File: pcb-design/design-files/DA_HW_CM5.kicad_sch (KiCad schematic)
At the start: 13 parts, among them J4 USB_A, J5 ComputeModule5-CM5_UnitA, J6 ComputeModule5-CM5_UnitB, U6 TPS2041CDBV

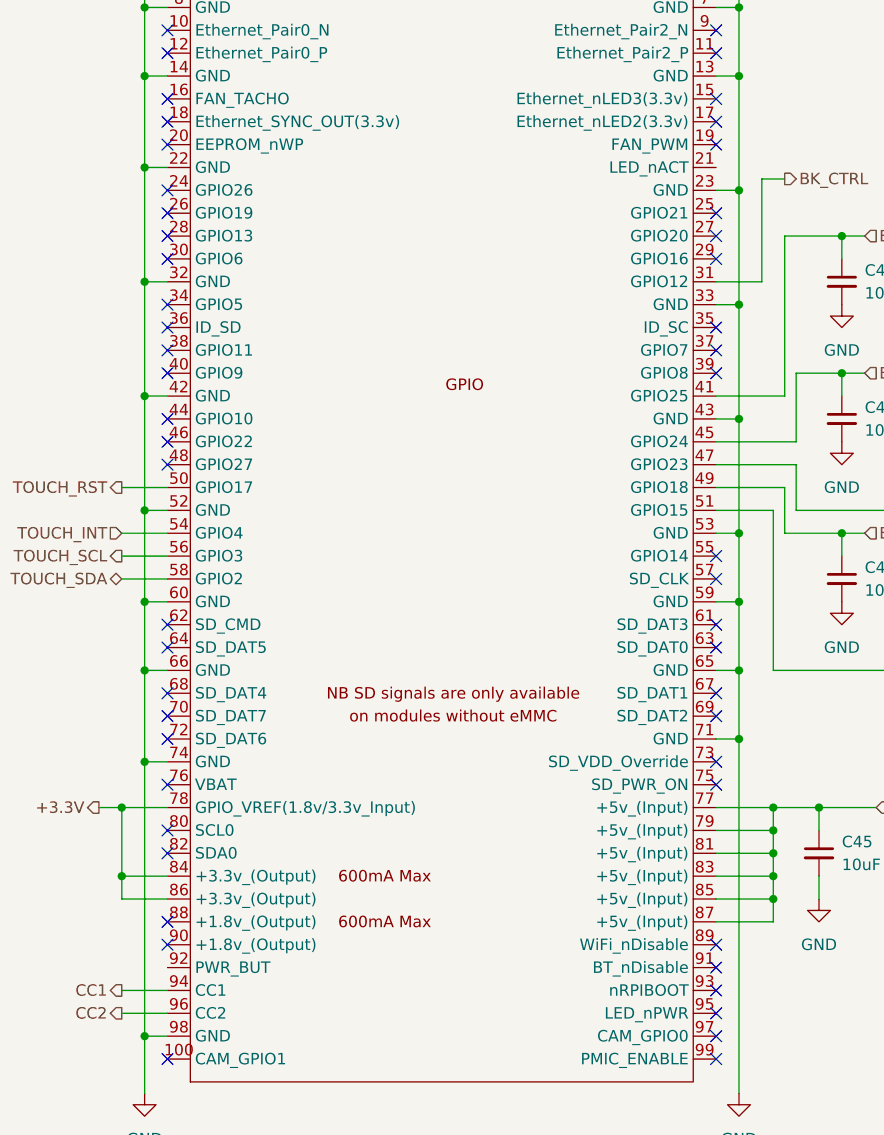
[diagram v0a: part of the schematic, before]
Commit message: Fix HW rev B issues
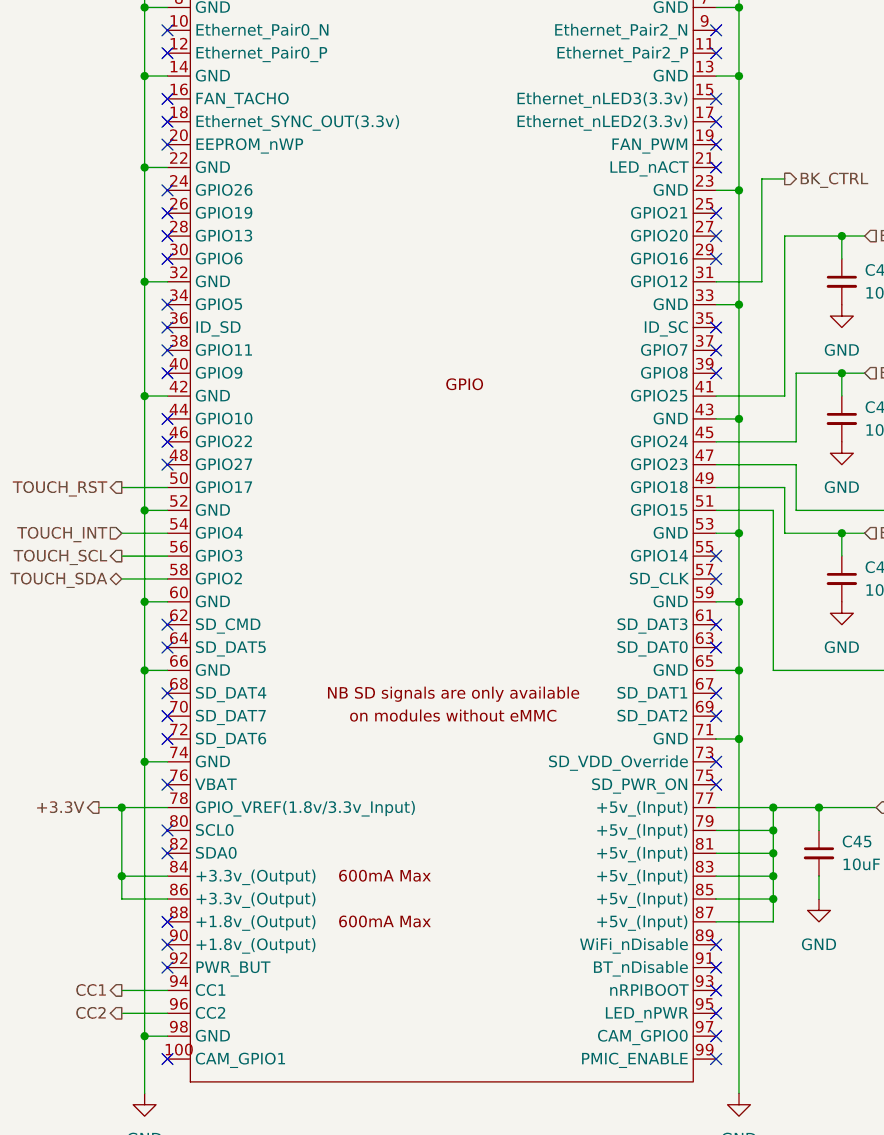
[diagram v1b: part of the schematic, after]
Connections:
- no-connect marks 116 -> 118
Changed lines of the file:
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@@
+	)
+	(no_connect
+		(at 33.02 143.51)
 	)
 	(no_connect
@@
 	)
 	(no_connect
+		(at 93.98 54.61)
+	)
+	(no_connect

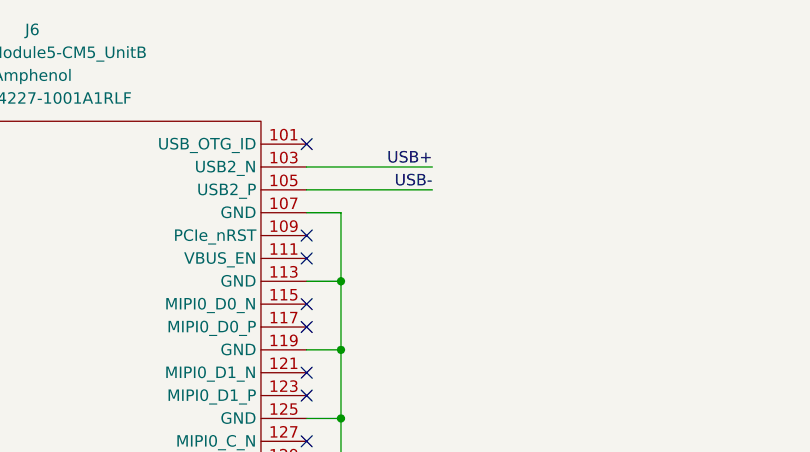
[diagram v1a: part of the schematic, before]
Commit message: Fix USB D+ and D- connections
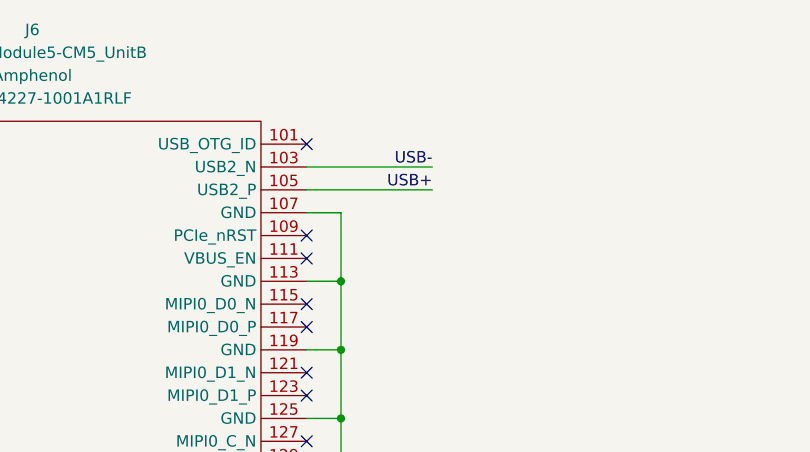
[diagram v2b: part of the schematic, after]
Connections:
- net USB+: now also J6.105 (USB2_P); no longer J6.103 (USB2_N)
- net USB-: now also J6.103 (USB2_N); no longer J6.105 (USB2_P)
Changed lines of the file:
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@@
 	)
 	(label "USB+"
-		(at 219.71 31.75 180)
+		(at 219.71 34.29 180)
 		(effects
 			(font
@@
 	)
 	(label "USB-"
-		(at 219.71 34.29 180)
+		(at 219.71 31.75 180)
 		(effects
 			(font
